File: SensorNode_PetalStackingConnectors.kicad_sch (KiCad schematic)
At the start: 4 parts, among them J4 10132797-031100LF, J5 10132797-031100LF, SW2 SW_Push

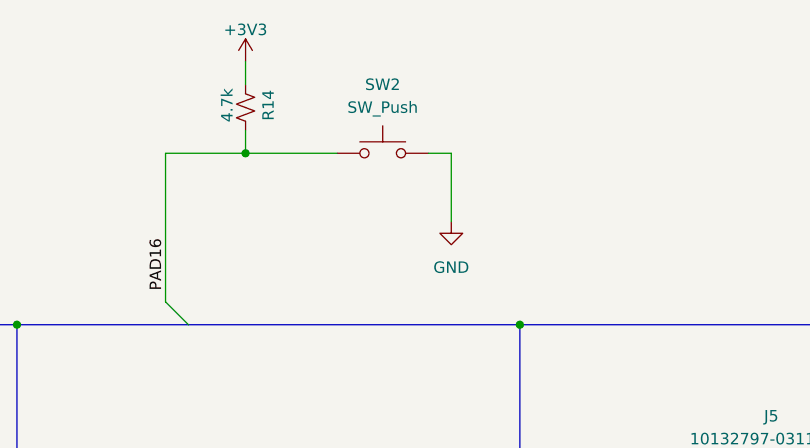
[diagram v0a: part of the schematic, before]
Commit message: replaced soil_sns frontend with SN74
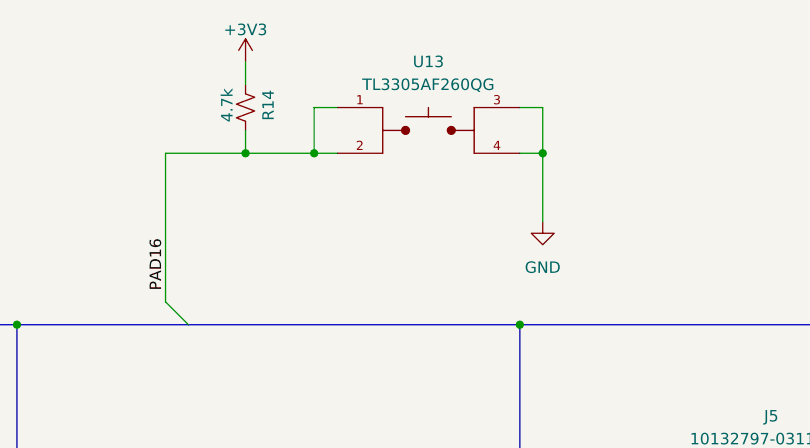
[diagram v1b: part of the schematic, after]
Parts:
- removed SW2: SW_Push, symbol Switch:SW_Push
- added U13: TL3305AF260QG, SproutSenseFootprints:SW_TL3305AF260QG, symbol SproutSense:TL3305AF260QG
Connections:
- net GND: now also U13.3, U13.4
- net PAD16: now also U13.1, U13.2
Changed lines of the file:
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@@
+	)
+	(junction
+		(at 175.26 48.26)
+		(diameter 0)
+		(color 0 0 0 0)
 	)
 	(junction
@@
 	)
 	(junction
+		(at 149.86 48.26)
+		(diameter 0)
+		(color 0 0 0 0)
+	)
+	(junction
 		(at 102.87 107.95)
 		(diameter 0)
@@
 	(wire
 		(pts
+			(xy 172.72 43.18) (xy 175.26 43.18)
+		)
+		(stroke
+			(width 0)
+			(type default)
+		)
+	)
+	(wire
+		(pts
 			(xy 213.36 105.41) (xy 223.52 105.41)
 		)
@@
 	(wire
 		(pts
-			(xy 152.4 48.26) (xy 142.24 48.26)
+			(xy 175.26 43.18) (xy 175.26 48.26)
+		)
+		(stroke
+			(width 0)
+			(type default)
+		)
+	)
+	(wire
+		(pts
+			(xy 152.4 48.26) (xy 149.86 48.26)
 		)
 		(stroke
@@
 	(wire
 		(pts
-			(xy 165.1 48.26) (xy 165.1 55.88)
+			(xy 175.26 48.26) (xy 175.26 55.88)
 		)
 		(stroke
@@
 	(wire
 		(pts
-			(xy 162.56 48.26) (xy 165.1 48.26)
+			(xy 172.72 48.26) (xy 175.26 48.26)
 		)
 		(stroke
@@
 	(wire
 		(pts
+			(xy 149.86 48.26) (xy 142.24 48.26)
+		)
+		(stroke
+			(width 0)
+			(type default)
+		)
+	)
+	(wire
+		(pts
+			(xy 152.4 43.18) (xy 149.86 43.18)
+		)
+		(stroke
+			(width 0)
+			(type default)
+		)
+	)
+	(wire
+		(pts
 			(xy 177.8 97.79) (xy 187.96 97.79)
 		)
@@
 		(pts
 			(xy 67.31 92.71) (xy 76.2 92.71)
+		)
+		(stroke
+			(width 0)
+			(type default)
+		)
+	)
+	(wire
+		(pts
+			(xy 149.86 43.18) (xy 149.86 48.26)
 		)
 		(stroke
@@
 			)
 			(justify left)
-		)
-	)
-	(symbol
-		(lib_id "Switch:SW_Push")
-		(at 157.48 48.26 0)
-		(unit 1)
-		(exclude_from_sim no)
-		(in_bom yes)
-		(on_board yes)
-		(dnp no)
-		(property "Reference" "SW2"
-			(at 157.48 40.64 0)
-			(effects
-				(font
-					(size 1.27 1.27)
-				)
-			)
-		)
-		(property "Value" "SW_Push"
-			(at 157.48 43.18 0)
-			(effects
-				(font
-					(size 1.27 1.27)
-				)
-			)
-		)
-		(property "Footprint" ""
-			(at 157.48 43.18 0)
-			(effects
-				(font
-					(size 1.27 1.27)
-				)
-				(hide yes)
-			)
-		)
-		(property "Datasheet" "~"
-			(at 157.48 43.18 0)
-			(effects
-				(font
-					(size 1.27 1.27)
-				)
-				(hide yes)
-			)
-		)
-		(property "Description" "Push button switch, generic, two pins"
-			(at 157.48 48.26 0)
-			(effects
-				(font
-					(size 1.27 1.27)
-				)
-				(hide yes)
-			)
-		)
-		(pin "1"
-		)
-		(pin "2"
-		)
-		(instances
-			(project "SproutSync_SensorNode"
-				(path "/6b347550-6a02-4d2d-97d7-e1cbb1403859/25175014-0a25-4d25-a8eb-172d74801ff1"
-					(reference "SW2")
-					(unit 1)
-				)
-			)
 		)
 	)
@@
 	)
 	(symbol
+		(lib_id "SproutSense:TL3305AF260QG")
+		(at 162.56 45.72 0)
+		(unit 1)
+		(exclude_from_sim no)
+		(in_bom yes)
+		(on_board yes)
+		(dnp no)
+		(fields_autoplaced yes)
+		(property "Reference" "U13"
+			(at 162.56 38.1 0)
+			(effects
+				(font
+					(size 1.27 1.27)
+				)
+			)
+		)
+		(property "Value" "TL3305AF260QG"
+			(at 162.56 40.64 0)
+			(effects
+				(font
+					(size 1.27 1.27)
+				)
+			)
+		)
+		(property "Footprint" "SproutSenseFootprints:SW_TL3305AF260QG"
+			(at 162.56 45.72 0)
+			(effects
+				(font
+					(size 1.27 1.27)
+				)
+				(justify bottom)
+				(hide yes)
+			)
+		)
+		(property "Datasheet" "https://configured-product-images.s3.amazonaws.com/Datasheets/TL3305.pdf"
+			(at 162.56 45.72 0)
+			(effects
+				(font
+					(size 1.27 1.27)
+				)
+				(hide yes)
+			)
+		)
+		(property "Description" "SWITCH TACTILE SPST-NO 0.05A 12V"
+			(at 162.56 45.72 0)
+			(effects
+				(font
+					(size 1.27 1.27)
+				)
+				(hide yes)
+			)
+		)
+		(property "PARTREV" "C"
+			(at 162.56 45.72 0)
+			(effects
+				(font
+					(size 1.27 1.27)
+				)
+				(justify bottom)
+				(hide yes)
+			)
+		)
+		(property "MANUFACTURER" "E-Switch"
+			(at 162.56 45.72 0)
+			(effects
+				(font
+					(size 1.27 1.27)
+				)
+				(justify bottom)
+				(hide yes)
+			)
+		)
+		(property "MAXIMUM_PACKAGE_HEIGHT" "3.8mm"
+			(at 162.56 45.72 0)
+			(effects
+				(font
+					(size 1.27 1.27)
+				)
+				(justify bottom)
+				(hide yes)
+			)
+		)
+		(property "STANDARD" "Manufacturer recommendations"
+			(at 162.56 45.72 0)
+			(effects
+				(font
+					(size 1.27 1.27)
+				)
+				(justify bottom)
+				(hide yes)
+			)
+		)
+		(property "Distributor Prt #" "EG5353CT-ND"
+			(at 162.56 45.72 0)
+			(effects
+				(font
+					(size 1.27 1.27)
+				)
+				(hide yes)
+			)
+		)
+		(property "Manuf Prt #" "TL3305AF260QG"
+			(at 162.56 45.72 0)
+			(effects
+				(font
+					(size 1.27 1.27)
+				)
+				(hide yes)
+			)
+		)
+		(pin "1"
+		)
+		(pin "2"
+		)
+		(pin "3"
+		)
+		(pin "4"
+		)
+		(instances
+			(project "SproutSync_SensorNode"
+				(path "/6b347550-6a02-4d2d-97d7-e1cbb1403859/25175014-0a25-4d25-a8eb-172d74801ff1"
+					(reference "U13")
+					(unit 1)
+				)
+			)
+		)
+	)
+	(symbol
 		(lib_id "power:GND")
-		(at 165.1 55.88 0)
+		(at 175.26 55.88 0)
 		(unit 1)
 		(exclude_from_sim no)
@@
 		(fields_autoplaced yes)
 		(property "Reference" "#PWR057"
-			(at 165.1 62.23 0)
+			(at 175.26 62.23 0)
 			(effects
 				(font
@@
 		)
 		(property "Value" "GND"
-			(at 165.1 60.96 0)
+			(at 175.26 60.96 0)
 			(effects
 				(font
@@
 		)
 		(property "Footprint" ""
-			(at 165.1 55.88 0)
+			(at 175.26 55.88 0)
 			(effects
 				(font
@@
 		)
 		(property "Datasheet" ""
-			(at 165.1 55.88 0)
+			(at 175.26 55.88 0)
 			(effects
 				(font
@@
 		)
 		(property "Description" "Power symbol creates a global label with name \"GND\" , ground"
-			(at 165.1 55.88 0)
-			(effects
-				(font
+			(at 175.26 55.88 0)
+			(effects
+				(font

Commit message: ver2 layout in progress
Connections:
- net PAD0: now reaches J4.1
- net PAD6: now reaches J4.20
- net PAD8: now reaches J4.22
- net PAD37: now reaches J4.23
- net PAD10: now reaches J4.25
- net PAD9: now reaches J4.26
- net PAD23: now reaches J4.3
- net PAD24: now reaches J4.4
- net PAD26: now reaches J4.5
- net PAD25: now reaches J4.8
- net PAD5: now reaches J4.9

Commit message: updated schematic for pwr savings
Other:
- title: SproutSyncProto-A-01 -> SproutSyncProto-A-02

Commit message: updated pcb for pwr savings
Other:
- title: SproutSyncProto-A-02 -> SproutSyncProto-A-04
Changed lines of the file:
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@@
 	(paper "A4")
 	(title_block
-		(title "SproutSyncProto-A-02")
-		(date "2026-04-29")
+		(title "SproutSyncProto-A-04")
+		(date "2026-05-04")
 		(rev "0.2")
 		(company "SproutSync LTD")
